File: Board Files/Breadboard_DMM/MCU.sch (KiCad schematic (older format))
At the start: 17 parts

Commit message: Starting converting to hierachichal design
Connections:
- net labels added: ADC_DRDY, CALIBRATE_MUX_A, CALIBRATE_MUX_B, CALIBRATE_MUX_INH, CALIBRATE_MUX_RELAY_ON, METER_CURRENT_SOURCE_ON, SET_CURRENT_SOURCE_A, SET_CURRENT_SOURCE_B, VREF_4.096V_EN, ~SDHN_VREF_1.024V~
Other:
- note added: "Programming \nSwitch"
- note removed: "Programming Switch"
- moved on the sheet: C?, R?, SW?, U?

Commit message: Added new sheet for main supply measurement, added upgrades document
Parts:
- added R?: 100, symbol Device:R_US
- added U?: LCD-Generic_3.2in_SPI_SD, irex_Display:LCD-Generic-3.2in_89.30x55.04mm, symbol irex_Display_Graphic:LCD-Generic_3.2in_SPI_SD
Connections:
- net labels added: LCD_DC, LCD_~RESET~, SPI_LCD_CS, SPI_MISO, SPI_MOSI, SPI_SCK, SPI_SD_CS, ~VREF_1.024V_SHDN~
- net labels removed: ~SDHN_VREF_1.024V~
- wire segments 68 -> 102
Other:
- note added: "3.3V Regulator"
- note added: "Display"
- note added: "MCU"
- note added: "Programming Headers"
- moved on the sheet: C?, D?, J?, R?, SW?, U?

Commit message: Finished main design, cleaning up schematic
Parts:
- removed C? (x2): 1uF, symbol Device:C
- removed SW?: JS202011CQN, Button_Switch_THT:SW_CuK_JS202011CQN_DPDT_Straight, symbol Switch:SW_Push_DPDT
- removed U?: MIC5365-3.3YD5, Package_TO_SOT_SMD:SOT-23-5, symbol Regulator_Linear:MIC5365-3.3YD5
- added C? (x2): 0.1uF, symbol Device:C
- added J?: AudioJack3, symbol Connector:AudioJack3
- added U?: SI8422, Package_SO:SOIC-8_3.9x4.9mm_P1.27mm, symbol irex_Isolator:SI8422
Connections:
- net labels added: +5VL, ADC_~DRDY, GNDL, MCU_PROG_RX, MCU_PROG_TX, MCU_RX, MCU_TX, SCL_5V, SDA_5V, VREF_4.096V_~EN
- net labels removed: +5VD, ADC_DRDY, MCU_USART1_RX, MCU_USART1_TX, VREF_4.096V_EN, ~VREF_1.024V_SHDN~
- wire segments 102 -> 106
- no-connect marks 1 -> 6
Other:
- note added: "I2C Isolator"
- note added: "I2C Level Shifters"
- note removed: "3.3V Regulator"
- note removed: "Programming \nSwitch"
- moved on the sheet: C?, D?, J?, R?, SW?, U?

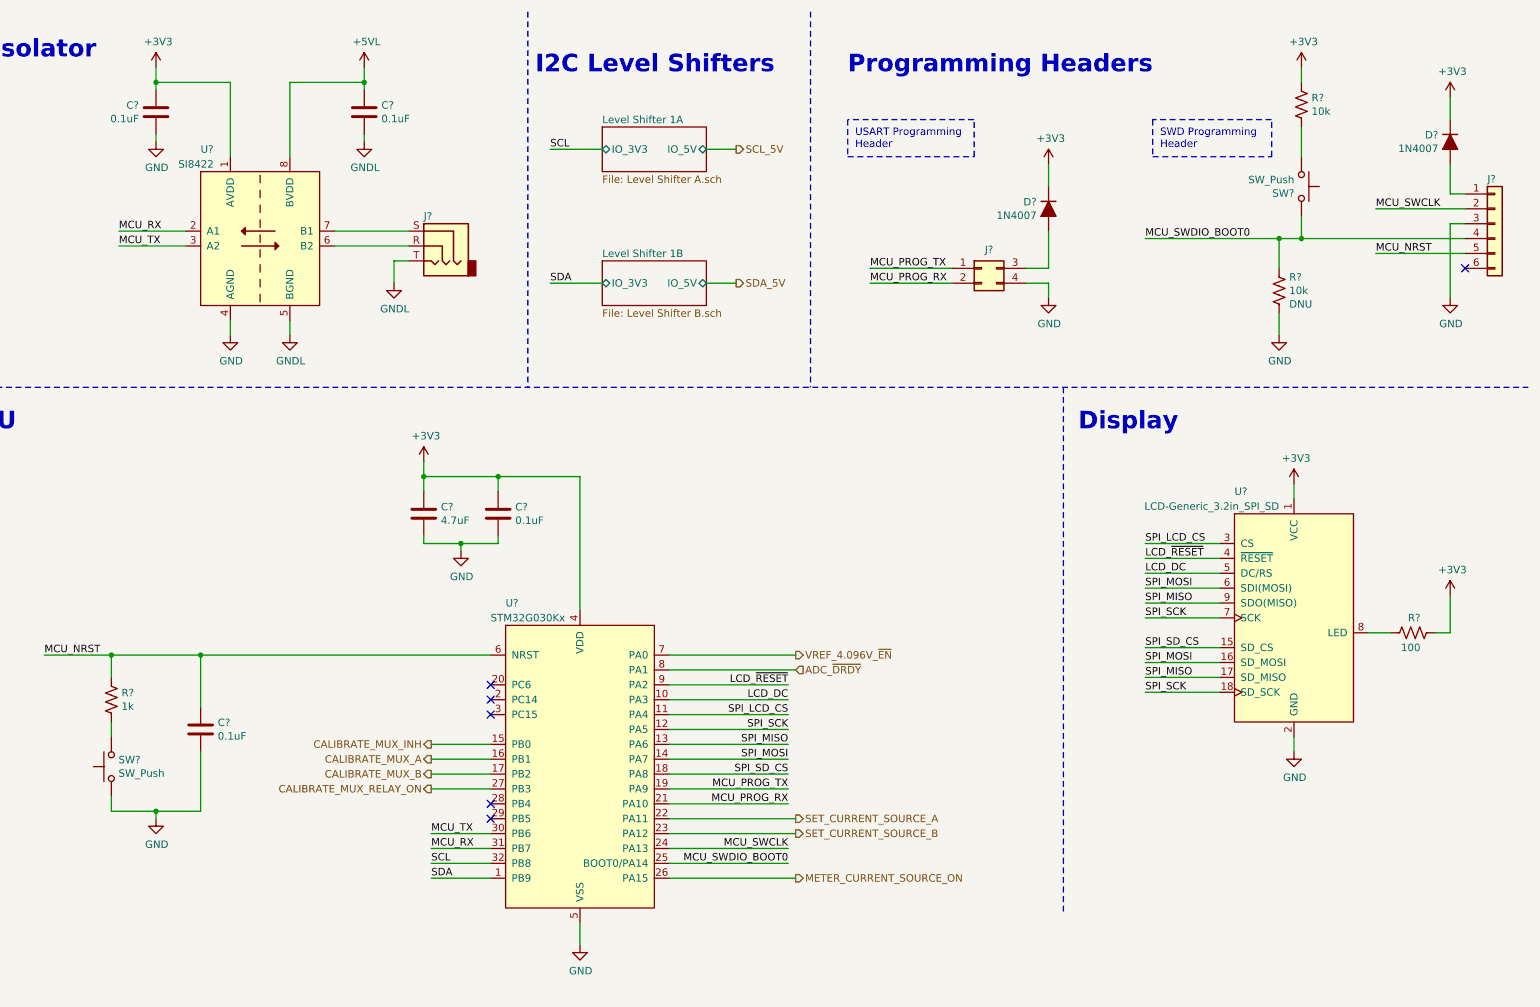
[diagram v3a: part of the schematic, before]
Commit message: Finished main cleanup, started adding digikey part numbers
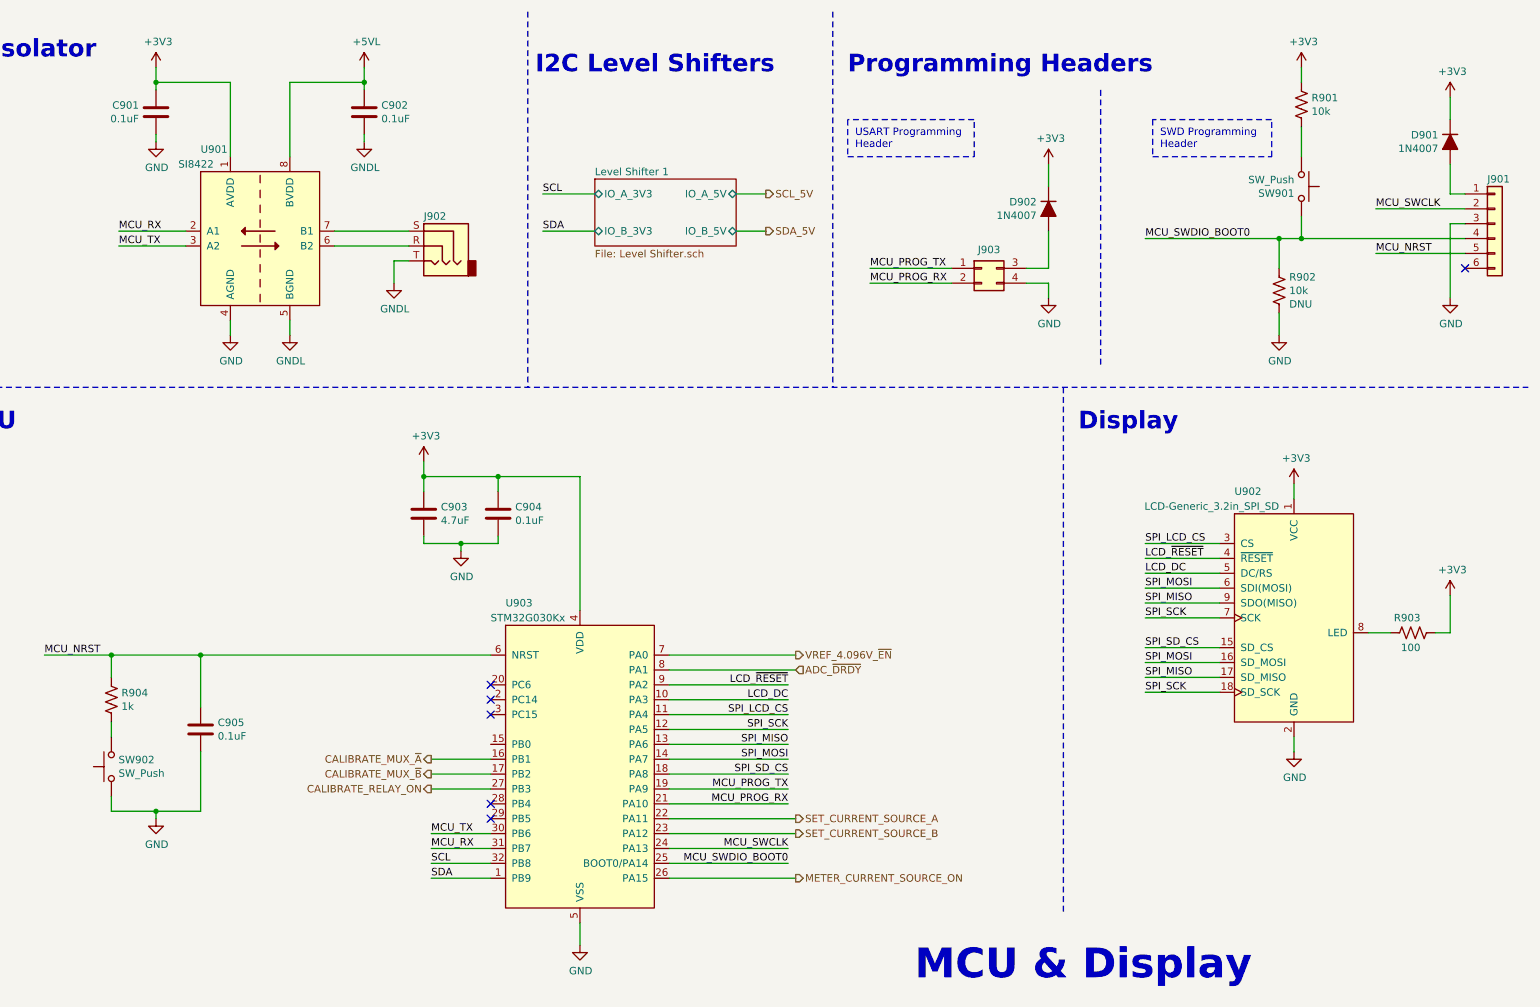
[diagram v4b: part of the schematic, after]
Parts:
- C901, C902, C904, C905: renamed from C?; Digi-Key PN (none) -> -
- C903: renamed from C?; Digi-Key Link (none) -> https://www.digikey.com/en/products/detail/samsung-electro-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; Digi-Key PN (none) -> 1276-6462-1-ND
- D901, D902: renamed from D?; Digi-Key PN (none) -> -
- J901, J902: renamed from J?; Digi-Key PN (none) -> -
- R901, R902, R903, R904: renamed from R?; Digi-Key PN (none) -> -
- SW901, SW902: renamed from SW?; Digi-Key PN (none) -> -
- U901, U902, U903: renamed from U?; Digi-Key PN (none) -> -
- gave numbers to parts that had none: 1
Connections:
- net CALIBRATE_MUX_A renamed CALIBRATE_MUX_~A
- net CALIBRATE_MUX_B renamed CALIBRATE_MUX_~B
- net CALIBRATE_MUX_INH: no longer names the net of U903.15 (PB0)
- net CALIBRATE_MUX_RELAY_ON renamed CALIBRATE_RELAY_ON
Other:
- note added: "MCU & Display"

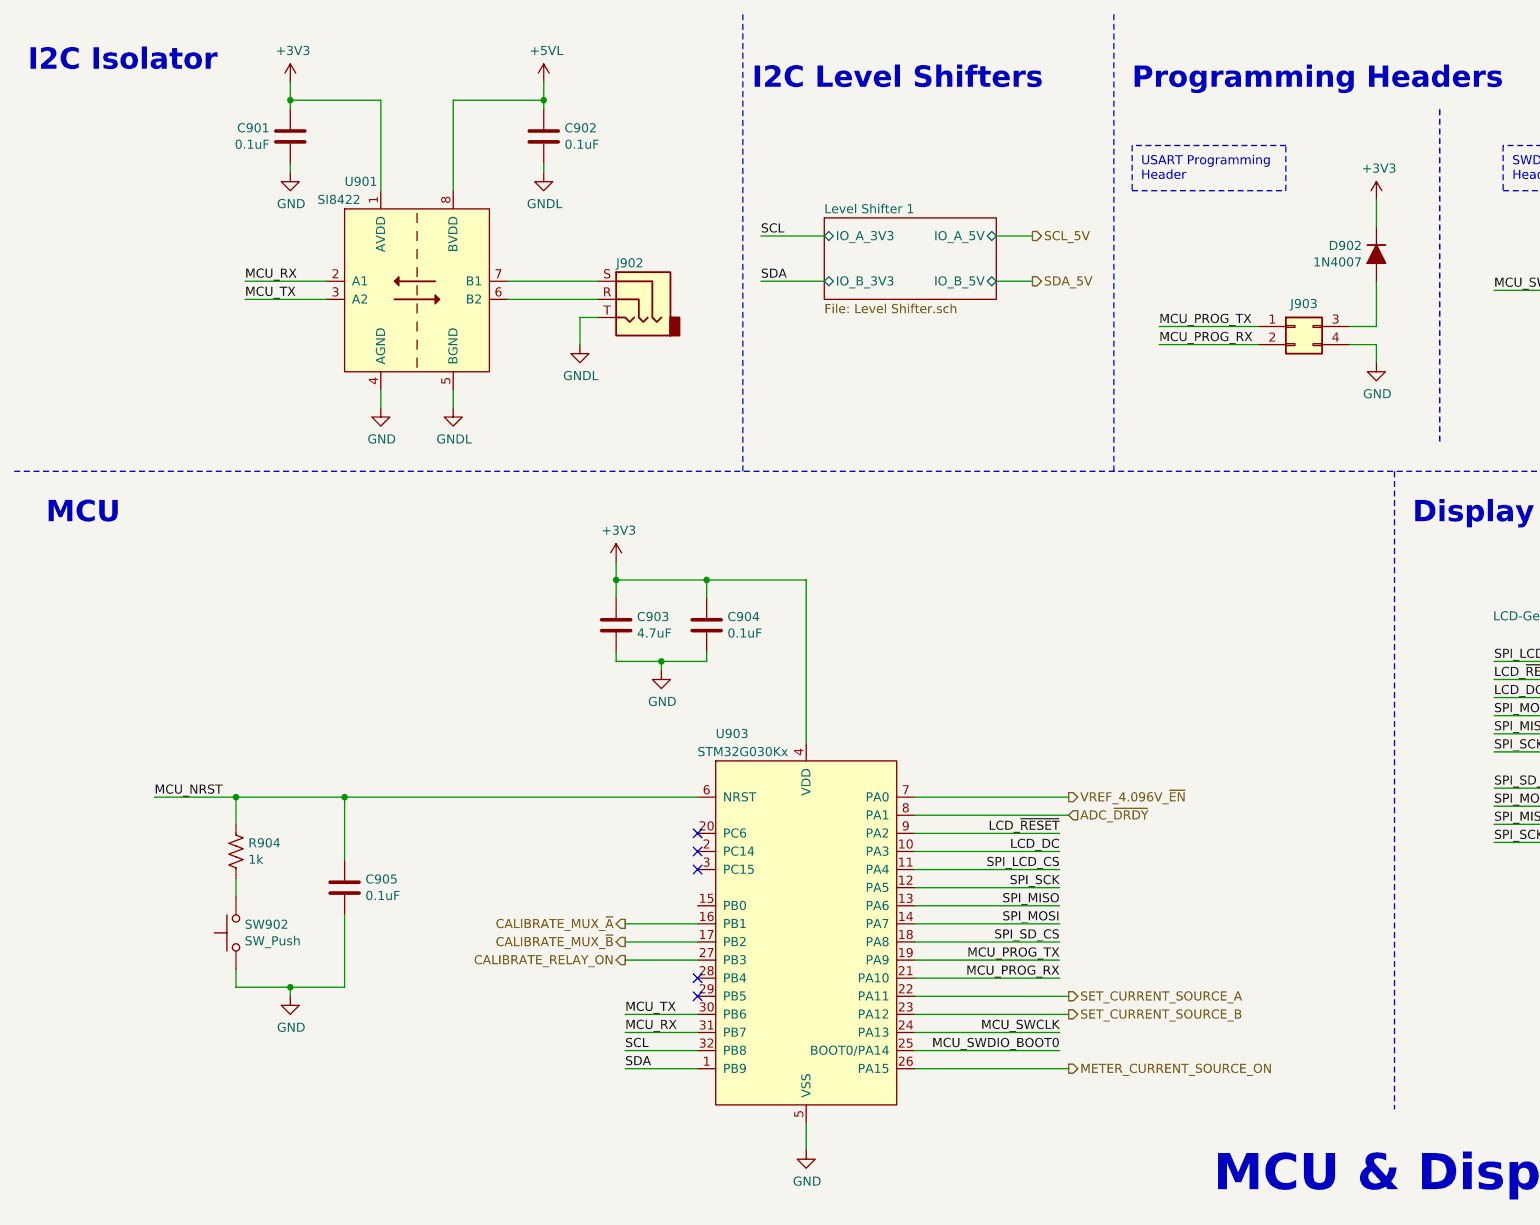
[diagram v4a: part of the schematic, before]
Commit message: Started adding Digikey links
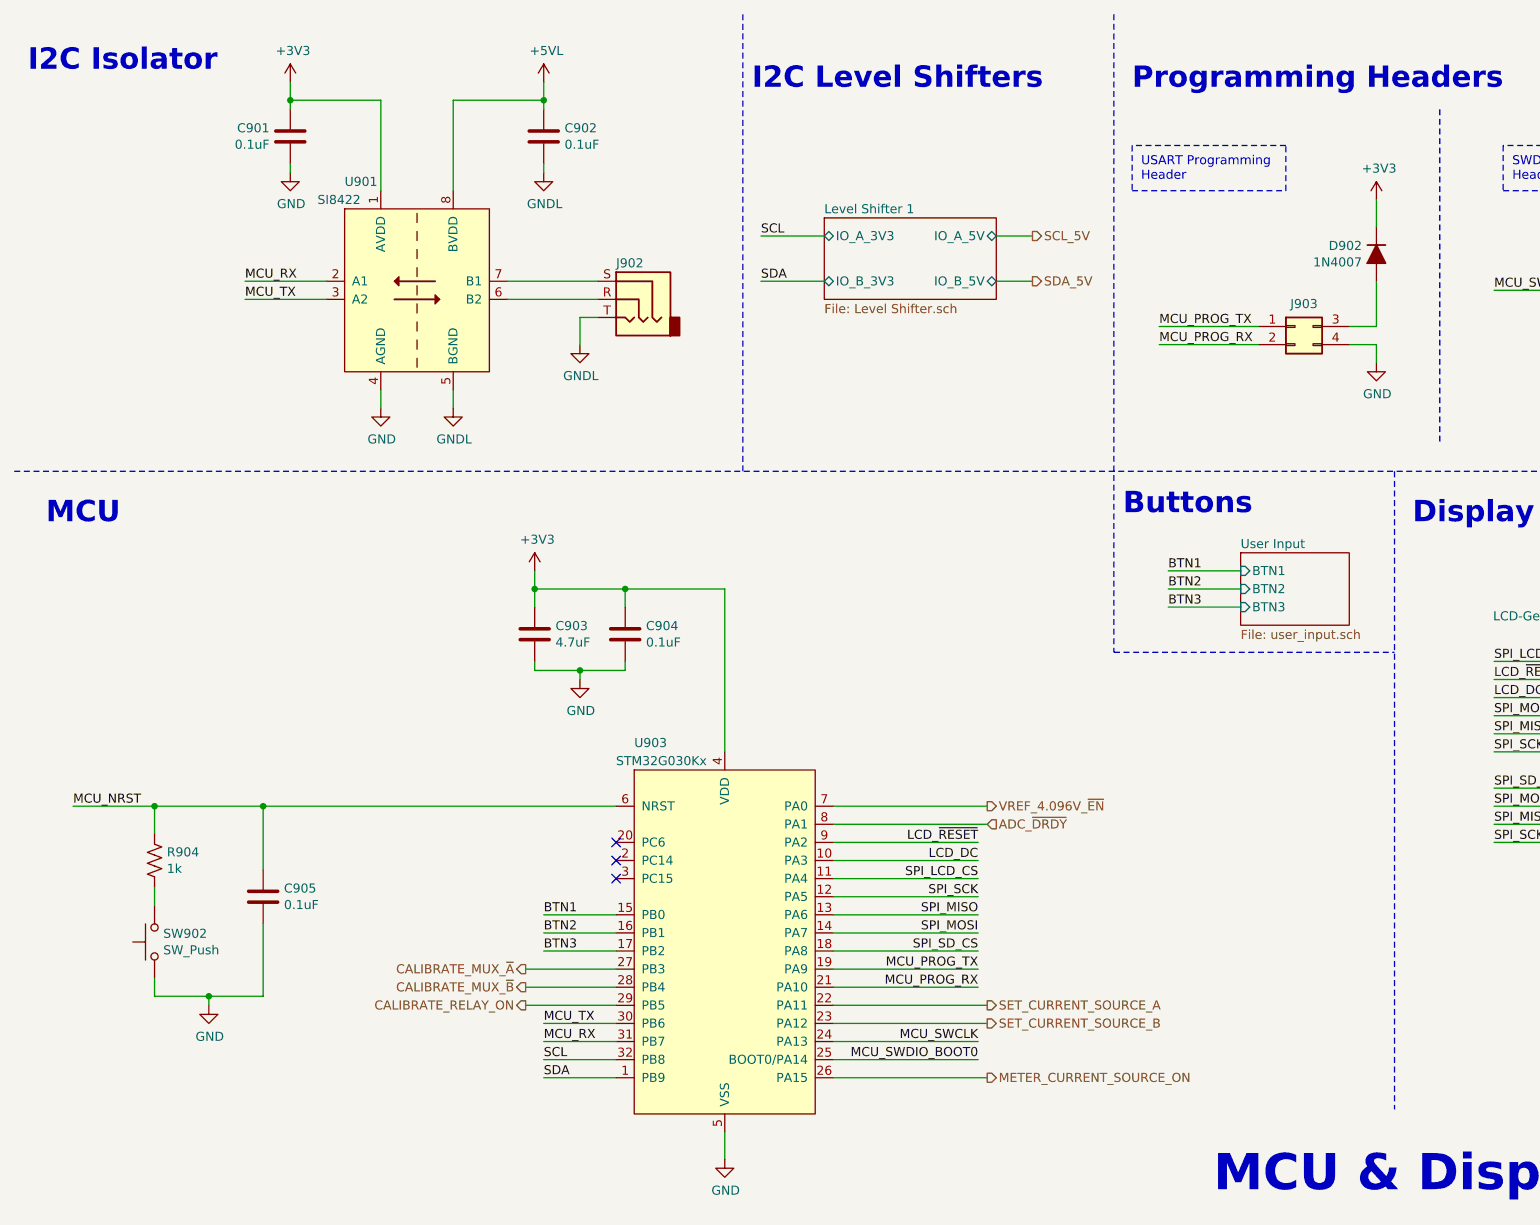
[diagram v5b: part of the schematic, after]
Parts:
- D901, D902: Digi-Key Link (none) -> https://www.digikey.com/en/products/detail/smc-diode-soluti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; Digi-Key PN - -> 1655-1N4007FLCT-ND
- J902: footprint (none) -> irex_Connector_Audio:Jack_3.5mm_CUI_SJ1-3523N_Horizontal; Digi-Key Link (none) -> https://www.digikey.com/en/products/detail/cui-devices/SJ1-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; Digi-Key PN - -> CP1-3523N-ND
- SW901, SW902: footprint (none) -> irex_Button_Switch_SMD:SW-PUSH-6x3.5mm_CK-PTS636SL43x_HandSolder; Digi-Key Link (none) -> https://www.digikey.com/en/products/detail/c-k/PTS636-SL43-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; Digi-Key PN - -> CKN12309-1-ND
- U901: Digi-Key Link (none) -> https://www.digikey.com/en/products/detail/silicon-labs/SI8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; Digi-Key PN - -> SI8422AB-D-IS-ND
- U902: Digi-Key Link (none) -> -
- U903: Digi-Key Link (none) -> https://www.digikey.com/en/products/detail/stmicroelectroni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; Digi-Key PN - -> 497-19769-ND
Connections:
- net CALIBRATE_MUX_~A: now also U903.27 (PB3); no longer U903.16 (PB1)
- net CALIBRATE_MUX_~B: now also U903.28 (PB4); no longer U903.17 (PB2)
- net CALIBRATE_RELAY_ON: now also U903.29 (PB5); no longer U903.27 (PB3)
- net BTN1: now reaches U903.15 (PB0)
- new net BTN2: U903.16 (PB1)
- new net BTN3: U903.17 (PB2)
- no-connect marks 6 -> 4
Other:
- note added: "Buttons"
- moved on the sheet: C903, C904, C905, R904, SW902, U903

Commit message: Finished adding parts, cleaned up, ran ERC
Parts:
- added C803, C806, C808: 0.1uF, Resistor_SMD:R_0603_1608Metric_Pad1.05x0.95mm_HandSolder, symbol Device:C
- added Q801: NTZD3154N, Package_TO_SOT_SMD:SOT-563, symbol irex_Transistor_FET:NTZD3154N
- added R801, R802, R805, R806: 4.7k, Resistor_SMD:R_0603_1608Metric_Pad1.05x0.95mm_HandSolder, symbol Device:R_US
- added R807, R809, R813: 10k, Resistor_SMD:R_0603_1608Metric_Pad1.05x0.95mm_HandSolder, symbol Device:R_US
- added R808, R812, R814: 1k, Resistor_SMD:R_0603_1608Metric_Pad1.05x0.95mm_HandSolder, symbol Device:R_US
- added SW802, SW803, SW805: SW_Push, irex_Button_Switch_SMD:SW_PUSH-12mm_Wuerth-430476085716_HandSolder, symbol Switch:SW_Push
- C801: renamed from C901; footprint (none) -> Resistor_SMD:R_0603_1608Metric_Pad1.05x0.95mm_HandSolder; Digi-Key Link (none) -> https://www.digikey.com/en/products/detail/samsung-electro-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; Digi-Key PN - -> 1276-1006-1-ND
- C802: renamed from C902; footprint (none) -> Resistor_SMD:R_0603_1608Metric_Pad1.05x0.95mm_HandSolder; Digi-Key Link (none) -> https://www.digikey.com/en/products/detail/samsung-electro-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; Digi-Key PN - -> 1276-1006-1-ND
- C804: renamed from C903; footprint (none) -> Resistor_SMD:R_0805_2012Metric_Pad1.15x1.40mm_HandSolder
- C805: renamed from C904; footprint (none) -> Resistor_SMD:R_0603_1608Metric_Pad1.05x0.95mm_HandSolder; Digi-Key Link (none) -> https://www.digikey.com/en/products/detail/samsung-electro-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; Digi-Key PN - -> 1276-1006-1-ND
- C807: renamed from C905; footprint (none) -> Resistor_SMD:R_0603_1608Metric_Pad1.05x0.95mm_HandSolder; Digi-Key Link (none) -> https://www.digikey.com/en/products/detail/samsung-electro-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; Digi-Key PN - -> 1276-1006-1-ND
- J801: renamed from J901; footprint (none) -> Connector_PinHeader_2.54mm:PinHeader_1x06_P2.54mm_Vertical; Digi-Key Link (none) -> https://www.digikey.com/en/products/detail/adam-tech/PH1-06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; Digi-Key PN - -> 2057-PH1-06-UA-ND
- J803: renamed from J903; footprint (none) -> Connector_PinHeader_2.54mm:PinHeader_2x02_P2.54mm_Vertical; Digi-Key Link (none) -> https://www.digikey.com/en/products/detail/adam-tech/PH2-04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; Digi-Key PN (none) -> 2057-PH2-04-UA-ND
- R803: renamed from R901; footprint (none) -> Resistor_SMD:R_0603_1608Metric_Pad1.05x0.95mm_HandSolder; Digi-Key Link (none) -> https://www.digikey.com/en/products/detail/yageo/RC0603FR-0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; Digi-Key PN - -> 311-10.0KHRCT-ND
- R804: renamed from R902; footprint (none) -> Resistor_SMD:R_0603_1608Metric_Pad1.05x0.95mm_HandSolder; Digi-Key Link (none) -> https://www.digikey.com/en/products/detail/yageo/RC0603FR-0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; Digi-Key PN - -> 311-10.0KHRCT-ND
- R810: renamed from R903; footprint (none) -> Resistor_SMD:R_0603_1608Metric_Pad1.05x0.95mm_HandSolder; Digi-Key Link (none) -> https://www.digikey.com/en/products/detail/yageo/RC0603FR-0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; Digi-Key PN - -> 311-100HRCT-ND
- R811: renamed from R904; footprint (none) -> Resistor_SMD:R_0603_1608Metric_Pad1.05x0.95mm_HandSolder; Digi-Key Link (none) -> https://www.digikey.com/en/products/detail/yageo/RC0603FR-0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; Digi-Key PN - -> 311-1.00KHRCT-ND
- U802: renamed from U902; Digi-Key Link - -> https://www.digikey.com/en/products/detail/samtec-inc/SLW-1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; Digi-Key PN - -> SAM1093-04-ND; SAM1093-14-ND
- renumbered D901 to D801, D902 to D802, J902 to J802, SW901 to SW801, SW902 to SW804, U901 to U801, U903 to U803
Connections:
- net +3V3: now also Q801.2 (G1), Q801.5 (G2), R801.1, R805.1, R807.1, R809.1, R813.1
- net BTN1: now also C803.1, R807.2, SW802.1
- net BTN2: now also C806.1, R809.2, SW803.1
- net BTN3: now also C808.1, R813.2, SW805.1
- net GND: now also C803.2, C806.2, C808.2, R808.2, R812.2, R814.2
- net SCL: now also Q801.1 (S1), R801.2
- net SCL_5V: now also Q801.6 (D1), R802.2
- net SDA: now also Q801.4 (S2), R805.2
- net SDA_5V: now also Q801.3 (D2), R806.2
- new net: R812.1, SW803.2
- new net: R814.1, SW805.2
- new net: R808.1, SW802.2
- new net +5VD: R802.1, R806.1
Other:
- note added: "UART Isolator"
- note removed: "I2C Isolator"
- moved on the sheet: C801, C802, C804, C805, C807, D801, D802, J801, J802, J803, R803, R804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
